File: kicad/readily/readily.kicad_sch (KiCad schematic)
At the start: 35 parts, among them J1 Conn_01x09_Socket, J3 USB_C_Receptacle_USB2.0_16P, SW2 SW_SPST, SW3 SW_SPST, U1 ESP32-S3-WROOM-1, U2 BQ24040DSQR, U3 TPD2EUSB30, U4 TLV75533PDRV, U5 WAFER-PH2_0-2PWZ, U7 ED08907M-FB15C7_0-C10-2049

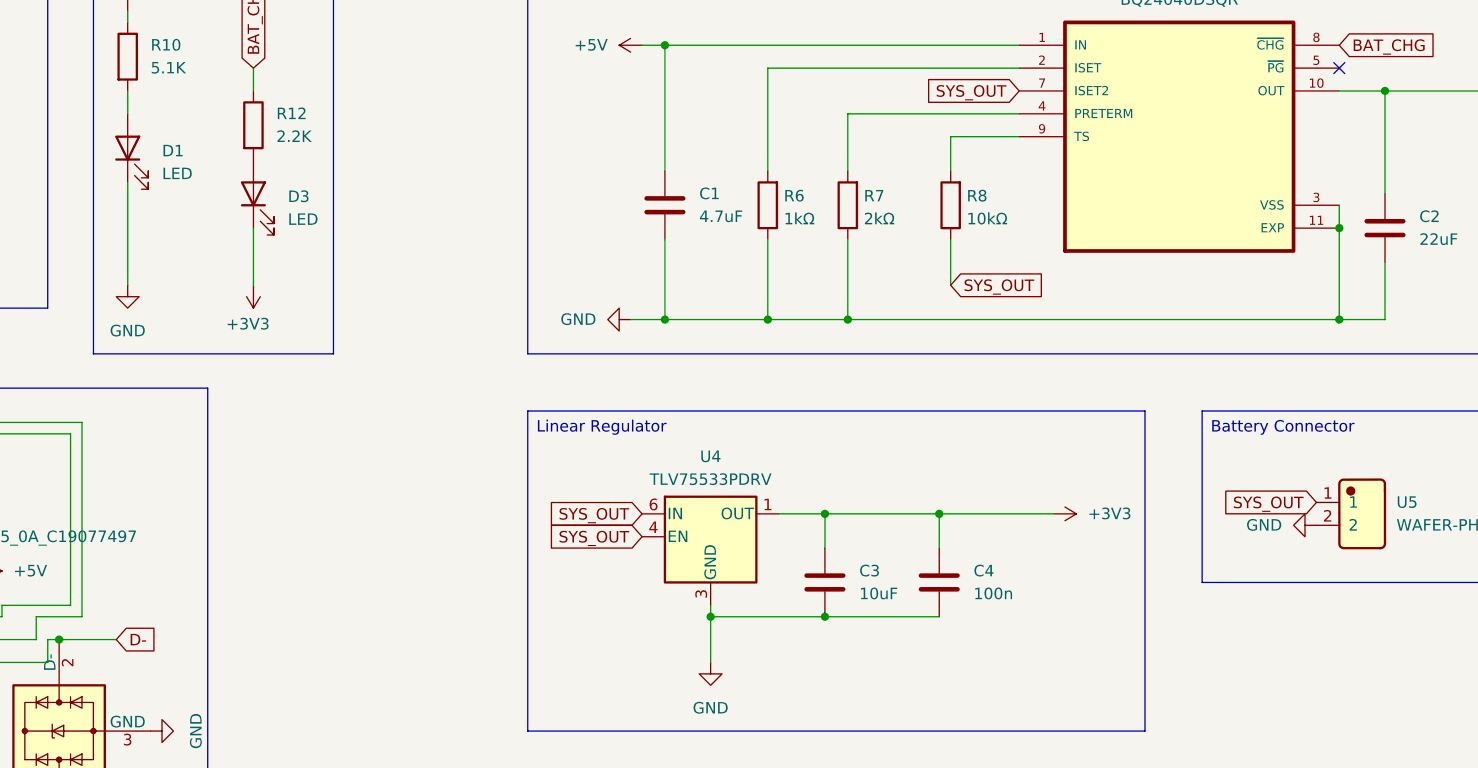
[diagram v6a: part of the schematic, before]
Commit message: feat: switching the battery JST and generating the final files for next print
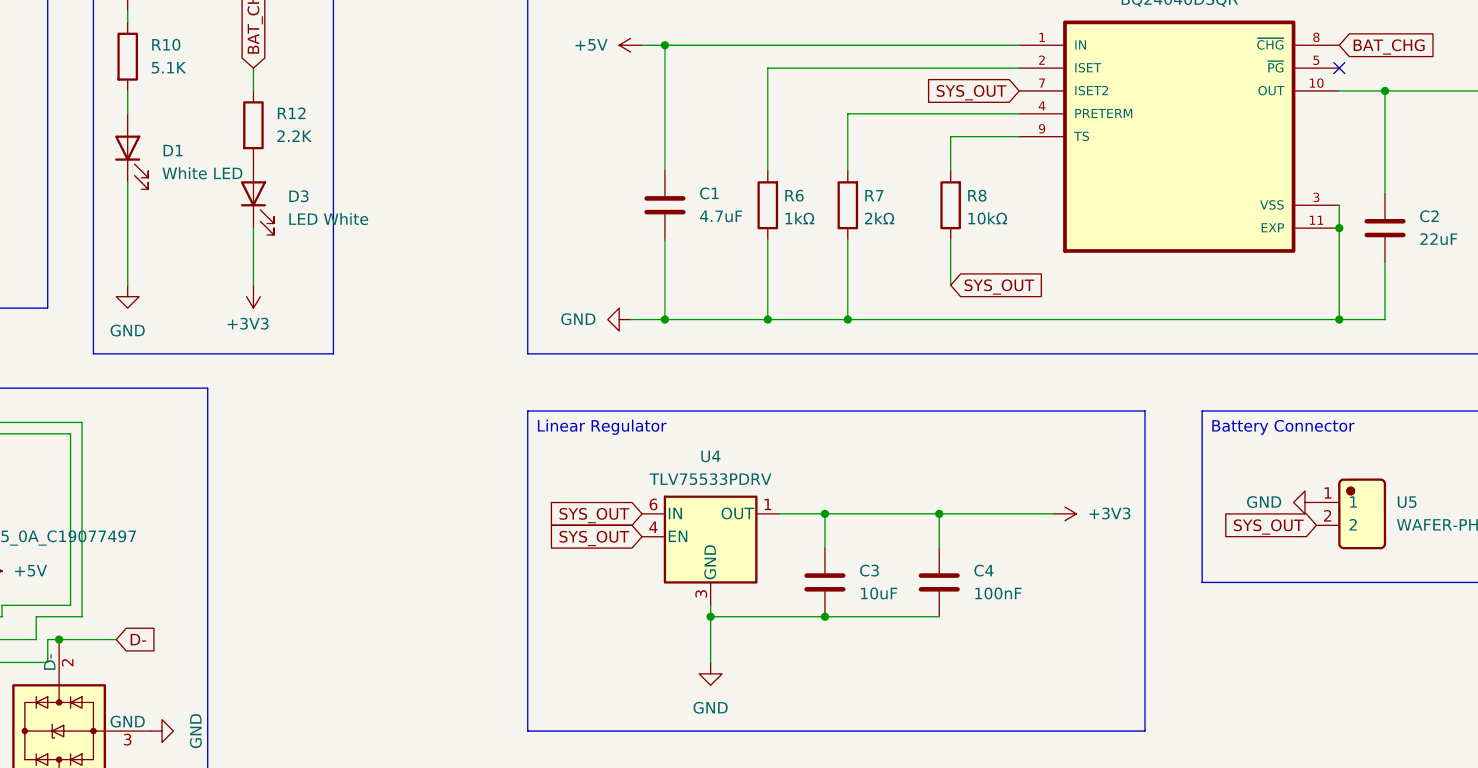
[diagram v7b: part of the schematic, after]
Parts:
- C4: value 100n -> 100nF
- D1: value LED -> White LED
- D3: value LED -> LED White
- J3: footprint Connector_USB:USB_C_Receptacle_HRO_TYPE-C-31-M-12 -> JLCImport:TYPE-C16PIN
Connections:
- net GND: now also U5.1; no longer U5.2
- net SYS_OUT: now also U5.2; no longer U5.1
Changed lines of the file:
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@@
 		)
 	)
+	(global_label "SYS_OUT"
+		(shape input)
+		(at 223.52 132.08 180)
+		(fields_autoplaced yes)
+		(effects
+			(font
+				(size 1.27 1.27)
+			)
+			(justify right)
+		)
+		(property "Intersheetrefs" "${INTERSHEET_REFS}"
+			(at 212.431 132.08 0)
+			(effects
+				(font
+					(size 1.27 1.27)
+				)
+				(justify right)
+				(hide yes)
+			)
+		)
+	)
 	(global_label "SD_CS"
 		(shape input)
@@
 		)
 	)
-	(global_label "SYS_OUT"
-		(shape input)
-		(at 223.52 129.54 180)
-		(fields_autoplaced yes)
-		(effects
-			(font
-				(size 1.27 1.27)
-			)
-			(justify right)
-		)
-		(property "Intersheetrefs" "${INTERSHEET_REFS}"
-			(at 212.431 129.54 0)
-			(effects
-				(font
-					(size 1.27 1.27)
-				)
-				(justify right)
-				(hide yes)
-			)
-		)
-	)
 	(global_label "SD_MOSI"
 		(shape input)
@@
 			)
 		)
-		(property "Value" "LED"
+		(property "Value" "White LED"
 			(at 95.25 93.0274 90)
 			(effects
@@
 			)
 		)
-		(property "Footprint" "Connector_USB:USB_C_Receptacle_HRO_TYPE-C-31-M-12"
+		(property "Footprint" "JLCImport:TYPE-C16PIN"
 			(at 52.07 152.4 0)
 			(effects
@@
 			)
 		)
-		(property "Value" "LED"
+		(property "Value" "LED White"
 			(at 109.22 98.1074 90)
 			(effects
@@
 	(symbol
 		(lib_id "power:GND")
-		(at 223.52 132.08 270)
+		(at 223.52 129.54 270)
 		(unit 1)
 		(exclude_from_sim no)
@@
 		(fields_autoplaced yes)
 		(property "Reference" "#PWR014"
-			(at 217.17 132.08 0)
+			(at 217.17 129.54 0)
 			(effects
 				(font
@@
 		)
 		(property "Value" "GND"
-			(at 219.71 132.0799 90)
+			(at 219.71 129.5399 90)
 			(effects
 				(font
@@
 		)
 		(property "Footprint" ""
-			(at 223.52 132.08 0)
+			(at 223.52 129.54 0)
 			(effects
 				(font
@@
 		)
 		(property "Datasheet" ""
-			(at 223.52 132.08 0)
+			(at 223.52 129.54 0)
 			(effects
 				(font
@@
 		)
 		(property "Description" "Power symbol creates a global label with name \"GND\" , ground"
-			(at 223.52 132.08 0)
+			(at 223.52 129.54 0)
 			(effects
 				(font
@@
 			)
 		)
-		(property "Value" "100n"
+		(property "Value" "100nF"
 			(at 185.42 139.6999 0)
 			(effects
